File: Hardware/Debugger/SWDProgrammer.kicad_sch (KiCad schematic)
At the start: 33 parts, among them J1 USB_C_Receptacle_USB2.0, U1 AP2112K-3.3, U2 STM32F103C8Tx, Y1 32.768KHZ, Y2 8Mhz

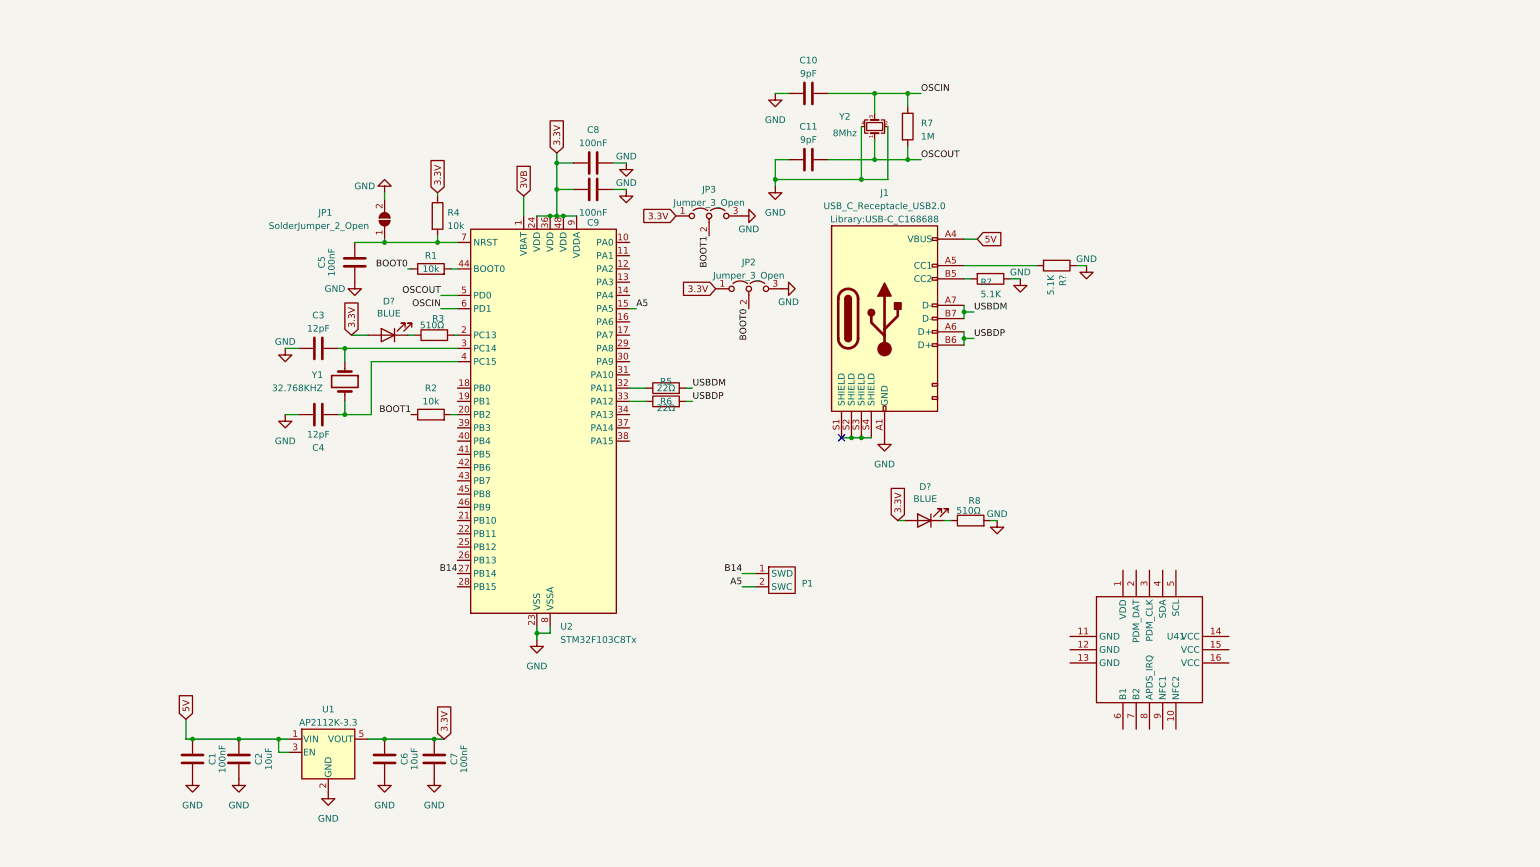
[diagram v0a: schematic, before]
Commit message: worked on debugger, has to be flipped
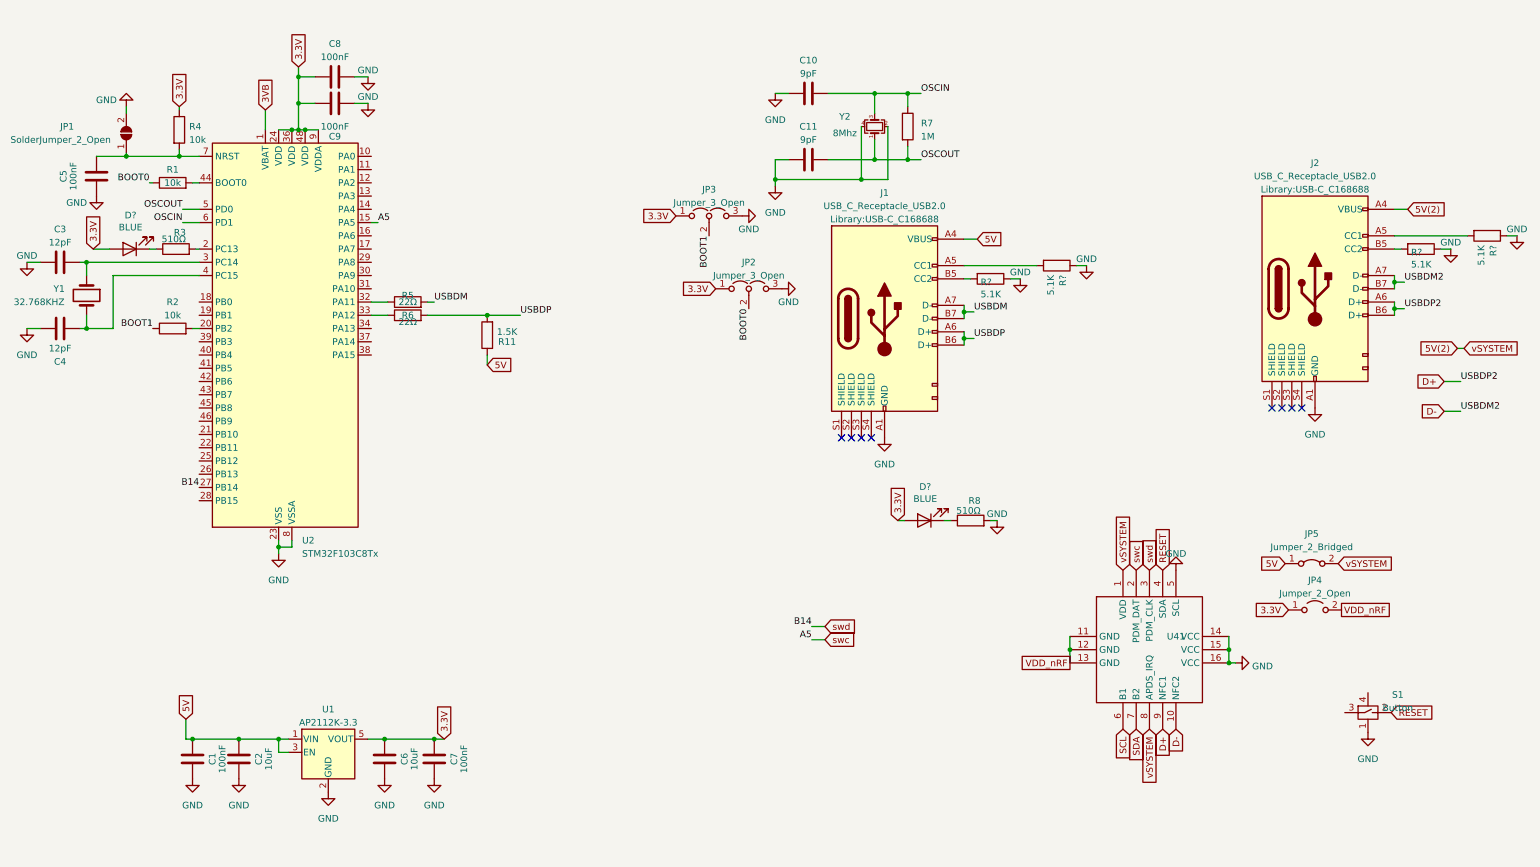
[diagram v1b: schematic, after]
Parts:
- removed P1: ~, Library:Programmer Pin, symbol Library:Programmer_Pin
- added J2: USB_C_Receptacle_USB2.0, Library:USB-C_C168688, symbol Library:USB_C_Receptacle_USB2.0
- added JP4: Jumper_2_Open, Jumper:SolderJumper-2_P1.3mm_Open_RoundedPad1.0x1.5mm, symbol Jumper:Jumper_2_Open
- added JP5: Jumper_2_Bridged, Jumper:SolderJumper-2_P1.3mm_Bridged_RoundedPad1.0x1.5mm, symbol Jumper:Jumper_2_Bridged
- added R11: 1.5K, Resistor_SMD:R_0402_1005Metric, symbol Device:R
- added R? (x2): 5.1K, Resistor_SMD:R_0402_1005Metric, symbol Device:R
- added S1: Button, Library:button 3x3, symbol Library:Button
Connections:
- net A5 is gone; now on net swc: U2.15 (PA5)
- net B14 is gone; now on net swd: U2.27 (PB14)
- net 3.3V: now also JP4.1 (A)
- net 5V: now also JP5.1 (A), R11.1
- net GND: now also U41.14 (VCC), U41.15 (VCC), U41.16 (VCC), U41.5 (SCL), J2.A1 (GND), R?.1, R?.1, S1.1
- net USBDP: now also R11.2
- net 5V(2): now reaches U41.1 (VDD)
- net 5V(2): now also U41.8 (APDS_IRQ), J2.A4 (VBUS), JP5.2 (B)
- net D-: now reaches U41.10 (NFC2)
- net D-: now also J2.A7 (D-), J2.B7 (D-)
- net VDD_nRF: now reaches U41.11 (GND)
- net VDD_nRF: now also U41.12 (GND), U41.13 (GND), JP4.2 (B)
- net swc: now reaches U41.2 (PDM_DAT)
- net swd: now reaches U41.3 (PDM_CLK)
- net RESET: now reaches U41.4 (SDA)
- net RESET: now also S1.2
- net SCL: now reaches U41.6 (B1)
- net SDA: now reaches U41.7 (B2)
- net D+: now reaches U41.9 (NFC1)
- net D+: now also J2.A6 (D+), J2.B6 (D+)
- new net: J2.A5 (CC1), R?.2
- new net: J2.B5 (CC2), R?.2
- now unconnected: J1.S1 (SHIELD), J1.S2 (SHIELD), J1.S3 (SHIELD), J1.S4 (SHIELD)
- no-connect marks 1 -> 8
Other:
- moved on the sheet: C3, C4, C5, C8, C9, D?, JP1, R1, R2, R3, R4, R5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

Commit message: finished debugger and wireless
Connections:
- net A9: now reaches U2.30 (PA9)
- net A10: now reaches U2.31 (PA10)
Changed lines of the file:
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@@
+    (effects (font (size 1.27 1.27)) (justify left bottom))
+  )
+  (label "A9" (at 86.36 64.77 0) (fields_autoplaced)
     (effects (font (size 1.27 1.27)) (justify left bottom))
   )
@@
     (effects (font (size 1.27 1.27)) (justify right bottom))
   )
+  (label "A10" (at 86.36 67.31 0) (fields_autoplaced)
+    (effects (font (size 1.27 1.27)) (justify left bottom))
+  )
   (label "OSCIN" (at 50.165 54.61 180) (fields_autoplaced)

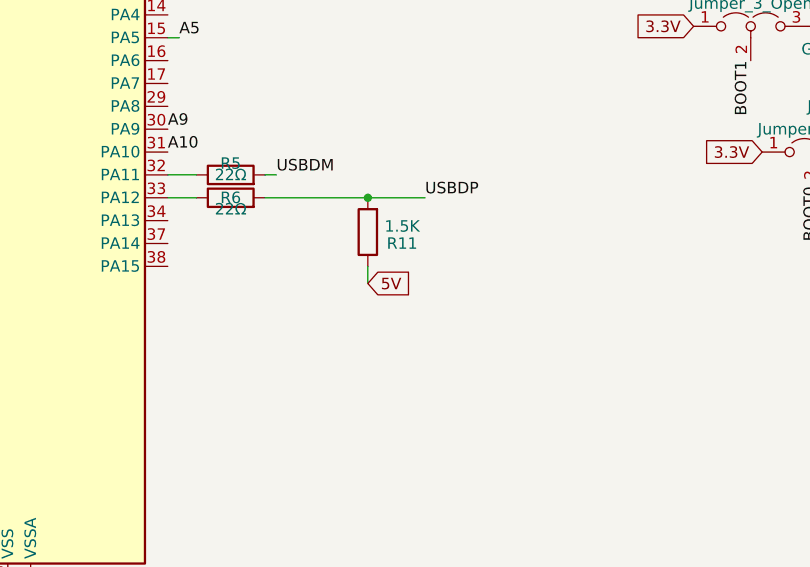
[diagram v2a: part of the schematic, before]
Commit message: fixed problems on debugger
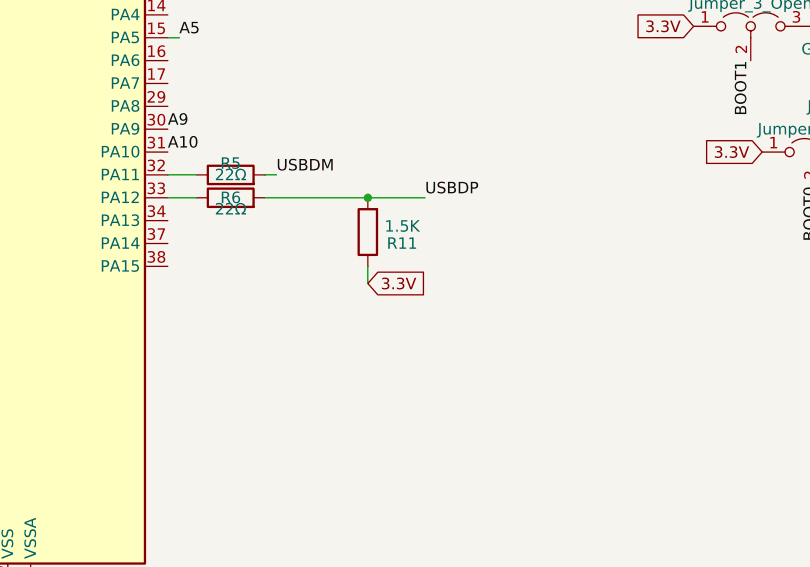
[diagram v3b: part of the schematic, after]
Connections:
- net 3.3V: now also R11.1
- net 5V: no longer R11.1
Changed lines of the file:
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@@
+    )
+  )
+  (global_label "3.3V" (shape input) (at 108.585 81.915 0) (fields_autoplaced)
+    (effects (font (size 1.27 1.27)) (justify left))
+    (property "Intersheetrefs" "${INTERSHEET_REFS}" (at 115.6032 81.915 0)
+      (effects (font (size 1.27 1.27)) (justify left) hide)
     )
   )
@@
       (effects (font (size 1.27 1.27)) (justify left) hide)
     )
-  )
-  (global_label "5V" (shape input) (at 108.585 81.915 0) (fields_autoplaced)
-    (effects (font (size 1.27 1.27)) (justify left))
-    (property "Intersheetrefs" "${INTERSHEET_REFS}" (at 113.7889 81.915 0)
-      (effects (font (size 1.27 1.27)) (justify left) hide)
-    )

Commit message: fixed design
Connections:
- net 3VB is gone; now on net 3.3V: U2.1 (VBAT)
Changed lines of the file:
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@@
   (junction (at 182.88 42.545) (diameter 0) (color 0 0 0 0)
+  )
+  (junction (at 68.58 36.83) (diameter 0) (color 0 0 0 0)
   )
   (junction (at 189.23 42.545) (diameter 0) (color 0 0 0 0)
@@
     (stroke (width 0) (type default))
   )
-  (wire (pts (xy 66.04 33.02) (xy 66.04 36.83))
-    (stroke (width 0) (type default))
-  )
   (wire (pts (xy 182.88 38.735) (xy 182.88 42.545))
     (stroke (width 0) (type default))
@@
     (stroke (width 0) (type default))
   )
+  (wire (pts (xy 66.04 36.83) (xy 68.58 36.83))
+    (stroke (width 0) (type default))
+  )
   (wire (pts (xy 210.82 65.405) (xy 208.915 65.405))
     (stroke (width 0) (type default))
@@
     )
   )
-  (global_label "3VB" (shape input) (at 66.04 33.02 90) (fields_autoplaced)
-    (effects (font (size 1.27 1.27)) (justify left))
-    (property "Intersheetrefs" "${INTERSHEET_REFS}" (at 66.04 26.5461 90)
-      (effects (font (size 1.27 1.27)) (justify left) hide)
-    )
-  )

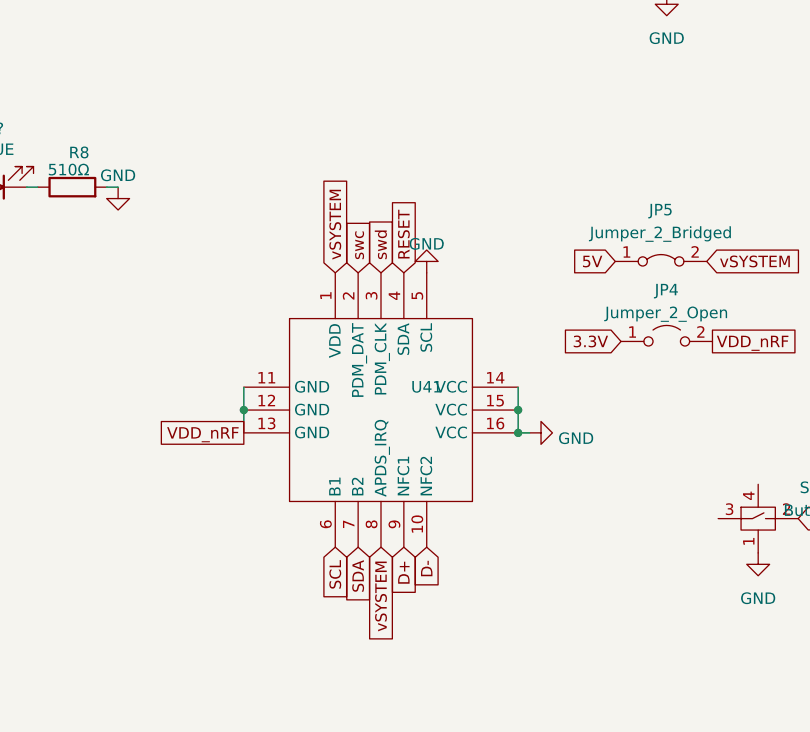
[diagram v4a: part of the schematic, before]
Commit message: added pogo charging pins, fixed debug connector
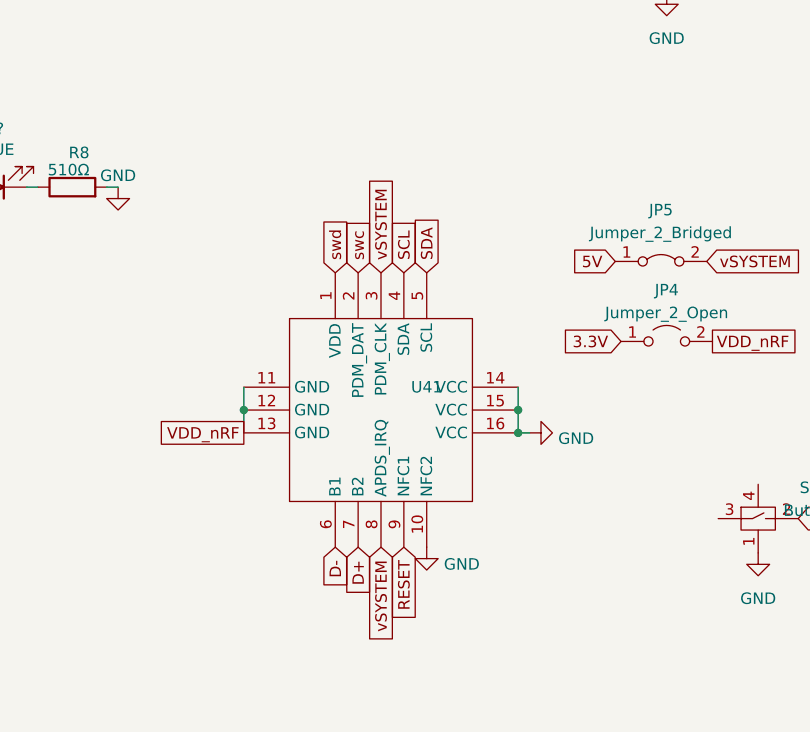
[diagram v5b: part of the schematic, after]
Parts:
- U41: footprint Library:BK13C06-10DS -> Library:BK13C06-10DP
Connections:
- net 5V(2): now also U41.3 (PDM_CLK); no longer U41.1 (VDD)
- net D+: now also U41.7 (B2); no longer U41.9 (NFC1)
- net D-: now also U41.6 (B1); no longer U41.10 (NFC2)
- net GND: now also U41.10 (NFC2); no longer U41.5 (SCL)
- net RESET: now also U41.9 (NFC1); no longer U41.4 (SDA)
- net SCL: now also U41.4 (SDA); no longer U41.6 (B1)
- net SDA: now also U41.5 (SCL); no longer U41.7 (B2)
- net swd: now also U41.1 (VDD); no longer U41.3 (PDM_CLK)

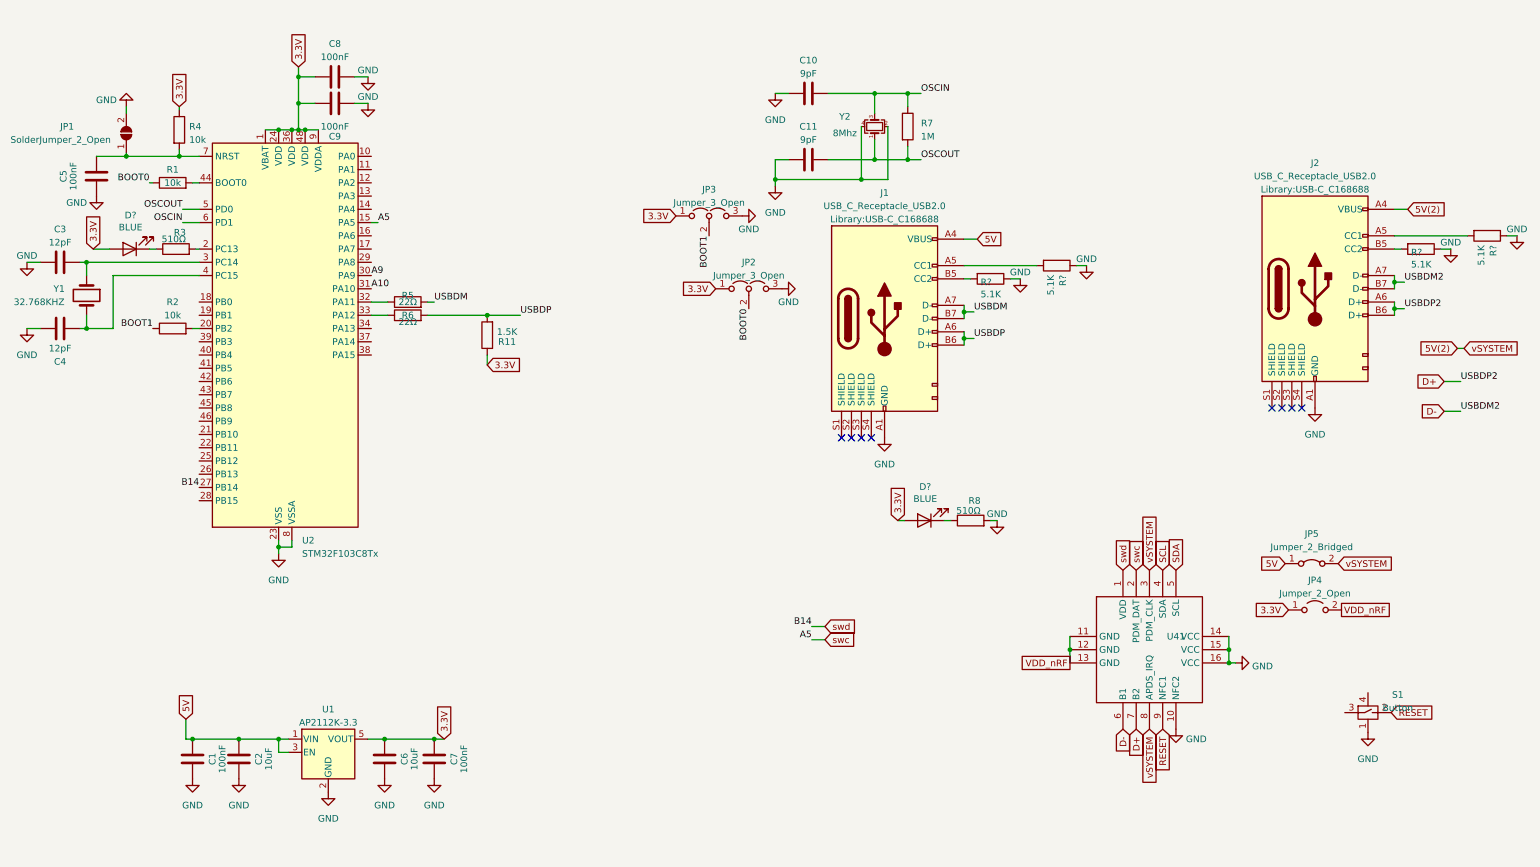
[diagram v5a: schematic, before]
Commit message: fixed some non existant bugs
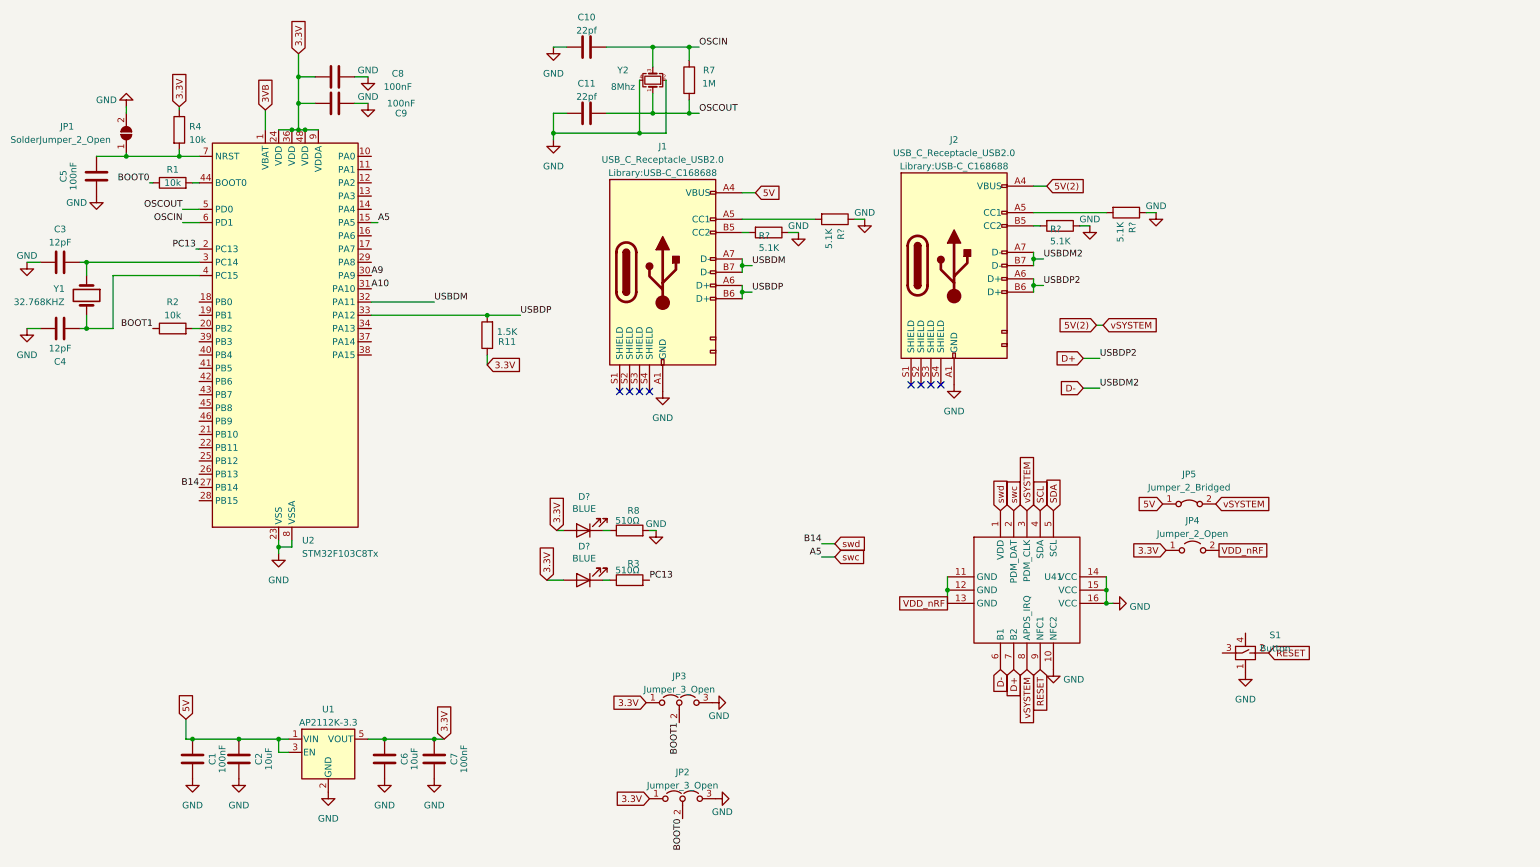
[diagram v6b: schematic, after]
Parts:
- removed R5, R6: 22Ω, Resistor_SMD:R_0402_1005Metric, symbol Device:R
- C10, C11: value 9pF -> 22pf
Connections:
- net 3.3V: no longer U2.1 (VBAT)
- net USBDM: now also U2.32 (PA11)
- net USBDP: now also U2.33 (PA12)
- net PC13: now reaches R3.2, U2.2 (PC13)
- new net 3VB: U2.1 (VBAT)
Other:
- moved on the sheet: C10, C11, D?, J1, J2, JP2, JP3, JP4, JP5, R3, R8, R?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

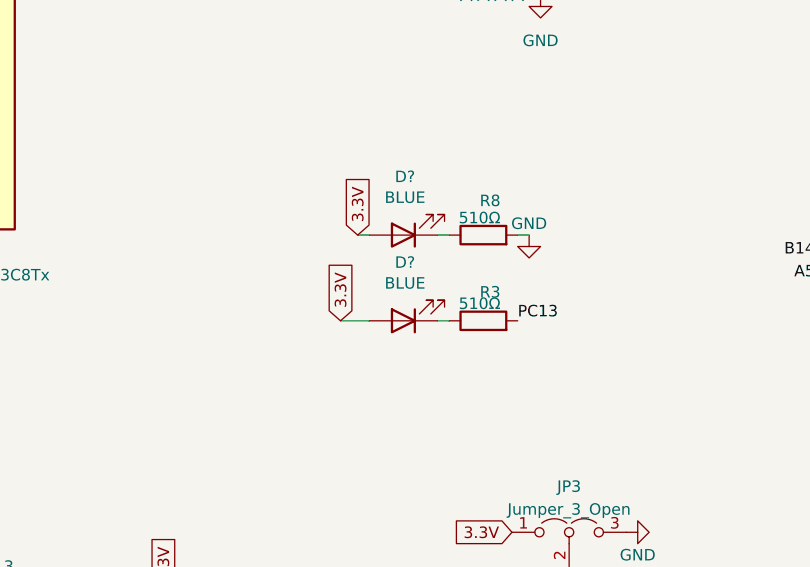
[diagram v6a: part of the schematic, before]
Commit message: added ID column
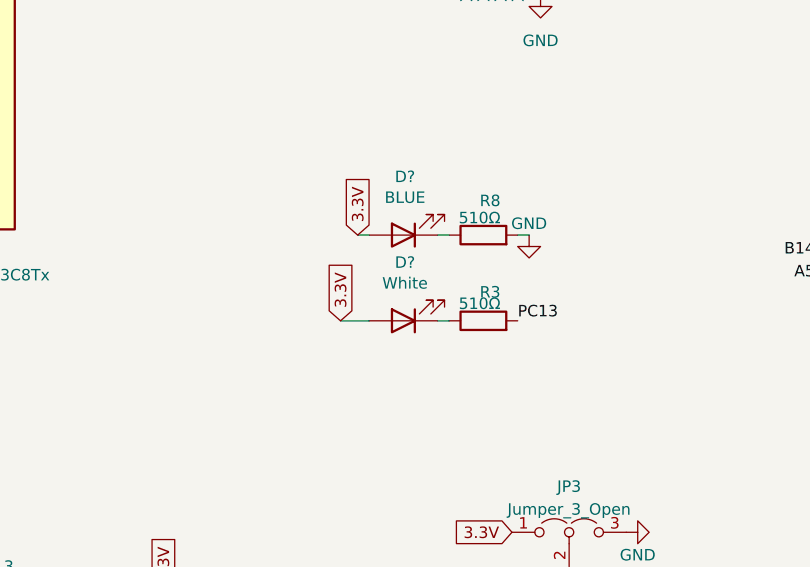
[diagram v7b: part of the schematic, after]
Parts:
- C1, C5, C7, C8, C9: ID (none) -> 21
- C10, C11: ID (none) -> 84
- C2, C6: ID (none) -> 83
- C3, C4: ID (none) -> 17
- D?: value BLUE -> White; ID (none) -> 97
- D?: ID (none) -> 90
- J1, J2: ID (none) -> 65
- R1, R2, R4: ID (none) -> 7
- R11: ID (none) -> 27
- R3, R8: ID (none) -> 100
- R7: ID (none) -> 28
- R? (x4): ID (none) -> 23
- S1: ID (none) -> 111
- U1: ID (none) -> 62
- U2: ID (none) -> 115
- Y1: ID (none) -> 43
- Y2: ID (none) -> 103
